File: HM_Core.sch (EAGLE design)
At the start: 7 parts

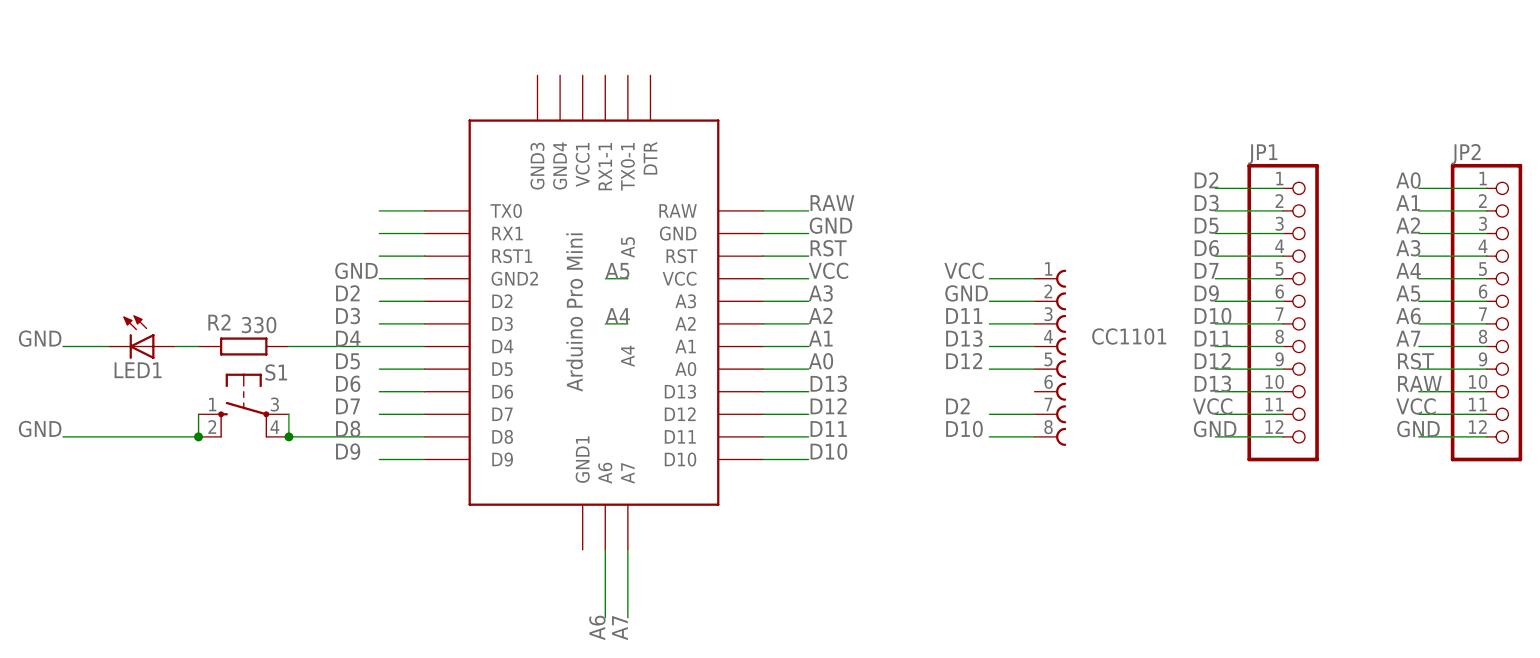
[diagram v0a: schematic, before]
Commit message: Verbesserungen
Taster zur seite raus
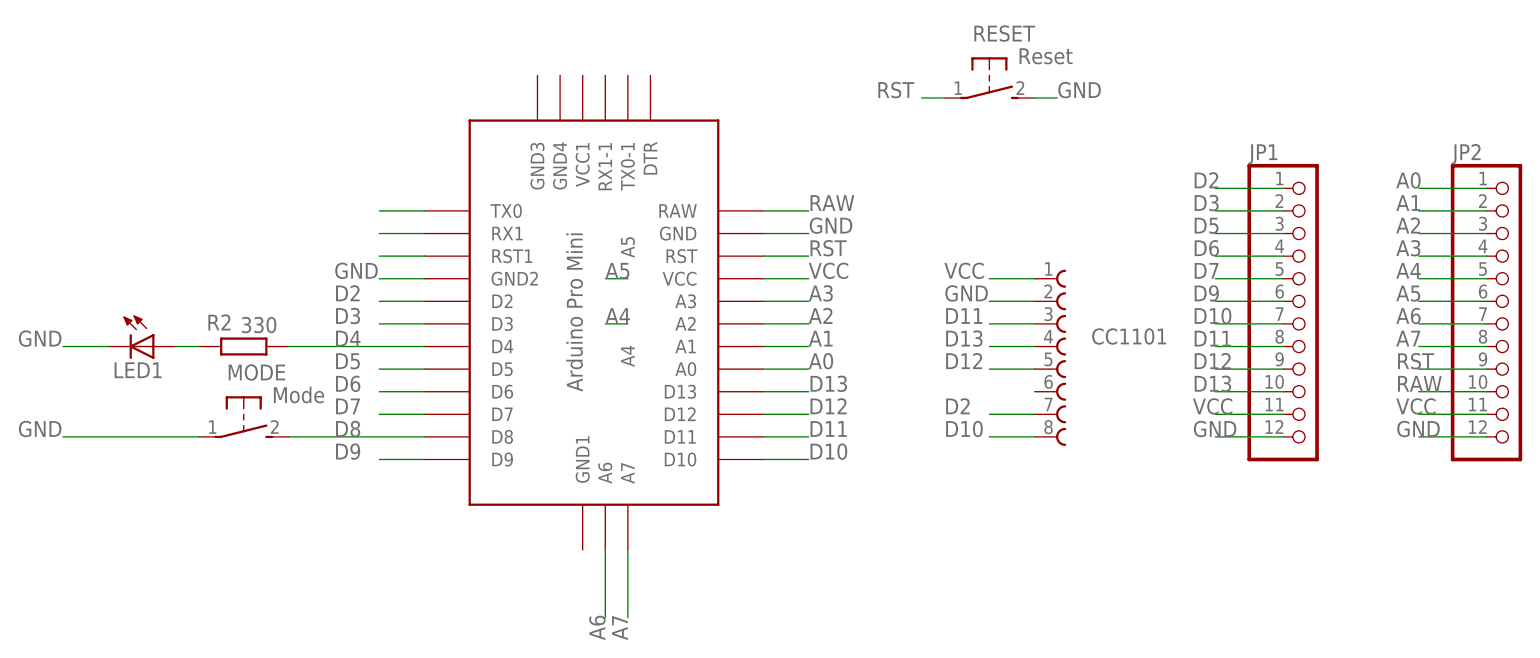
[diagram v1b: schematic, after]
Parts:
- removed S1: (no value), switch-omron:10-XX
- added MODE: Mode, switch-omron:31-XX
- added RESET: Reset, switch-omron:31-XX
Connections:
- net D8: now also MODE.S; no longer S1.P, S1.P1
- net GND: now also MODE.P, RESET.S; no longer S1.S, S1.S1
- net RST: now also RESET.P
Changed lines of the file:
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@@
 <grid distance="0.1" unitdist="inch" unit="inch" style="lines" multiple="1" display="no" altdistance="0.01" altunitdist="inch" altunit="inch"/>
 <layers>
-<layer number="1" name="Top" color="4" fill="1" visible="no" active="no"/>
-<layer number="16" name="Bottom" color="1" fill="1" visible="no" active="no"/>
-<layer number="17" name="Pads" color="2" fill="1" visible="no" active="no"/>
-<layer number="18" name="Vias" color="2" fill="1" visible="no" active="no"/>
-<layer number="19" name="Unrouted" color="6" fill="1" visible="no" active="no"/>
-<layer number="20" name="Dimension" color="15" fill="1" visible="no" active="no"/>
-<layer number="21" name="tPlace" color="7" fill="1" visible="no" active="no"/>
-<layer number="22" name="bPlace" color="7" fill="1" visible="no" active="no"/>
-<layer number="23" name="tOrigins" color="15" fill="1" visible="no" active="no"/>
-<layer number="24" name="bOrigins" color="15" fill="1" visible="no" active="no"/>
-<layer number="25" name="tNames" color="7" fill="1" visible="no" active="no"/>
-<layer number="26" name="bNames" color="7" fill="1" visible="no" active="no"/>
-<layer number="27" name="tValues" color="7" fill="1" visible="no" active="no"/>
-<layer number="28" name="bValues" color="7" fill="1" visible="no" active="no"/>
+<layer number="1" name="Top" color="4" fill="1" visible="yes" active="no"/>
+<layer number="16" name="Bottom" color="1" fill="1" visible="yes" active="no"/>
+<layer number="17" name="Pads" color="2" fill="1" visible="yes" active="no"/>
+<layer number="18" name="Vias" color="2" fill="1" visible="yes" active="no"/>
+<layer number="19" name="Unrouted" color="6" fill="1" visible="yes" active="no"/>
+<layer number="20" name="Dimension" color="24" fill="1" visible="yes" active="no"/>
+<layer number="21" name="tPlace" color="7" fill="1" visible="yes" active="no"/>
+<layer number="22" name="bPlace" color="7" fill="1" visible="yes" active="no"/>
+<layer number="23" name="tOrigins" color="15" fill="1" visible="yes" active="no"/>
+<layer number="24" name="bOrigins" color="15" fill="1" visible="yes" active="no"/>
+<layer number="25" name="tNames" color="7" fill="1" visible="yes" active="no"/>
+<layer number="26" name="bNames" color="7" fill="1" visible="yes" active="no"/>
+<layer number="27" name="tValues" color="7" fill="1" visible="yes" active="no"/>
+<layer number="28" name="bValues" color="7" fill="1" visible="yes" active="no"/>
 <layer number="29" name="tStop" color="7" fill="3" visible="no" active="no"/>
 <layer number="30" name="bStop" color="7" fill="6" visible="no" active="no"/>
@@
 <layer number="35" name="tGlue" color="7" fill="4" visible="no" active="no"/>
 <layer number="36" name="bGlue" color="7" fill="5" visible="no" active="no"/>
-<layer number="37" name="tTest" color="7" fill="1" visible="no" active="no"/>
-<layer number="38" name="bTest" color="7" fill="1" visible="no" active="no"/>
+<layer number="37" name="tTest" color="7" fill="1" visible="yes" active="no"/>
+<layer number="38" name="bTest" color="7" fill="1" visible="yes" active="no"/>
 <layer number="39" name="tKeepout" color="4" fill="11" visible="no" active="no"/>
 <layer number="40" name="bKeepout" color="1" fill="11" visible="no" active="no"/>
@@
 <layer number="44" name="Drills" color="7" fill="1" visible="no" active="no"/>
 <layer number="45" name="Holes" color="7" fill="1" visible="no" active="no"/>
-<layer number="46" name="Milling" color="3" fill="1" visible="no" active="no"/>
-<layer number="47" name="Measures" color="7" fill="1" visible="no" active="no"/>
-<layer number="48" name="Document" color="7" fill="1" visible="no" active="no"/>
-<layer number="49" name="Reference" color="7" fill="1" visible="no" active="no"/>
-<layer number="50" name="dxf" color="7" fill="1" visible="no" active="no"/>
-<layer number="51" name="tDocu" color="7" fill="1" visible="no" active="no"/>
-<layer number="52" name="bDocu" color="7" fill="1" visible="no" active="no"/>
-<layer number="53" name="tGND_GNDA" color="7" fill="9" visible="no" active="no"/>
-<layer number="54" name="bGND_GNDA" color="1" fill="9" visible="no" active="no"/>
-<layer number="56" name="wert" color="7" fill="1" visible="no" active="no"/>
-<layer number="57" name="tCAD" color="7" fill="1" visible="no" active="no"/>
-<layer number="59" name="tCarbon" color="7" fill="1" visible="no" active="no"/>
-<layer number="60" name="bCarbon" color="7" fill="1" visible="no" active="no"/>
+<layer number="46" name="Milling" color="3" fill="1" visible="yes" active="no"/>
+<layer number="47" name="Measures" color="7" fill="1" visible="yes" active="no"/>
+<layer number="48" name="Document" color="7" fill="1" visible="yes" active="no"/>
+<layer number="49" name="Reference" color="7" fill="1" visible="yes" active="no"/>
+<layer number="50" name="dxf" color="7" fill="1" visible="yes" active="no"/>
+<layer number="51" name="tDocu" color="7" fill="1" visible="yes" active="no"/>
+<layer number="52" name="bDocu" color="7" fill="1" visible="yes" active="no"/>
+<layer number="53" name="tGND_GNDA" color="7" fill="9" visible="yes" active="no"/>
+<layer number="54" name="bGND_GNDA" color="1" fill="9" visible="yes" active="no"/>
+<layer number="56" name="wert" color="7" fill="1" visible="yes" active="no"/>
+<layer number="57" name="tCAD" color="7" fill="1" visible="yes" active="no"/>
+<layer number="59" name="tCarbon" color="7" fill="1" visible="yes" active="no"/>
+<layer number="60" name="bCarbon" color="7" fill="1" visible="yes" active="no"/>
 <layer number="88" name="SimResults" color="9" fill="1" visible="yes" active="yes"/>
 <layer number="89" name="SimProbes" color="9" fill="1" visible="yes" active="yes"/>
@@
 <part name="R2" library="eagle-ltspice" library_urn="urn:adsk.eagle:library:217" deviceset="R" device="0207/10" package3d_urn="urn:adsk.eagle:package:13275/1" value="330"/>
 <part name="LED1" library="led" library_urn="urn:adsk.eagle:library:259" deviceset="LED" device="3MM" package3d_urn="urn:adsk.eagle:package:15797/1"/>
-<part name="S1" library="switch-omron" library_urn="urn:adsk.eagle:library:377" deviceset="10-XX" device="" package3d_urn="urn:adsk.eagle:package:27496/1"/>
 <part name="U$1" library="Arduino-clone" deviceset="ABK-PRO-MINI" device=""/>
 <part name="JP1" library="adafruit" library_urn="urn:adsk.eagle:library:420" deviceset="PINHD-1X12" device="" package3d_urn="urn:adsk.eagle:package:6240771/1"/>
 <part name="JP2" library="adafruit" library_urn="urn:adsk.eagle:library:420" deviceset="PINHD-1X12" device="" package3d_urn="urn:adsk.eagle:package:6240771/1"/>
 <part name="CC1101" library="Wurth_Elektronik_Electromechanic_Board_to_Board_Connectors_rev18b" library_urn="urn:adsk.eagle:library:7552989" deviceset="62000811121" device="" package3d_urn="urn:adsk.eagle:package:7553844/1"/>
+<part name="MODE" library="switch-omron" library_urn="urn:adsk.eagle:library:377" deviceset="31-XX" device="" package3d_urn="urn:adsk.eagle:package:27487/1" value="Mode"/>
+<part name="RESET" library="switch-omron" library_urn="urn:adsk.eagle:library:377" deviceset="31-XX" device="" package3d_urn="urn:adsk.eagle:package:27487/1" value="Reset"/>
 </parts>
 <sheets>
@@
 <attribute name="VALUE" x="-45.212" y="50.165" size="1.778" layer="96"/>
 </instance>
-<instance part="S1" gate="1" x="-30.48" y="48.26" smashed="yes" rot="MR270">
-<attribute name="NAME" x="-25.4" y="52.07" size="1.778" layer="95" rot="MR0"/>
-<attribute name="VALUE" x="-33.655" y="52.07" size="1.778" layer="96" rot="MR0"/>
-</instance>
 <instance part="U$1" gate="G$1" x="12.7" y="58.42" smashed="yes"/>
 <instance part="JP1" gate="G$1" x="88.9" y="60.96" smashed="yes">
@@
 <attribute name="NAME" x="64.77" y="56.118" size="1.778" layer="95"/>
 <attribute name="VALUE" x="64.77" y="53.34" size="1.778" layer="96"/>
+</instance>
+<instance part="MODE" gate="1" x="-30.48" y="45.72" smashed="yes" rot="R270">
+<attribute name="NAME" x="-32.385" y="52.07" size="1.778" layer="95"/>
+<attribute name="VALUE" x="-27.305" y="49.53" size="1.778" layer="96"/>
+</instance>
+<instance part="RESET" gate="1" x="53.34" y="83.82" smashed="yes" rot="R270">
+<attribute name="NAME" x="51.435" y="90.17" size="1.778" layer="95"/>
+<attribute name="VALUE" x="56.515" y="87.63" size="1.778" layer="96"/>
 </instance>
 </instances>
@@
 <net name="D8" class="0">
 <segment>
-<pinref part="S1" gate="1" pin="P"/>
 <wire x1="-10.16" y1="45.72" x2="-25.4" y2="45.72" width="0.1524" layer="91"/>
-<wire x1="-25.4" y1="45.72" x2="-25.4" y2="48.26" width="0.1524" layer="91"/>
-<pinref part="S1" gate="1" pin="P1"/>
-<junction x="-25.4" y="45.72"/>
 <pinref part="U$1" gate="G$1" pin="D8"/>
 <label x="-20.32" y="45.72" size="1.778" layer="95"/>
+<pinref part="MODE" gate="1" pin="S"/>
 </segment>
 </net>
@@
 </segment>
 <segment>
-<pinref part="S1" gate="1" pin="S"/>
-<wire x1="-35.56" y1="48.26" x2="-35.56" y2="45.72" width="0.1524" layer="91"/>
-<pinref part="S1" gate="1" pin="S1"/>
-<junction x="-35.56" y="45.72"/>
 <wire x1="-35.56" y1="45.72" x2="-50.8" y2="45.72" width="0.1524" layer="91"/>
 <label x="-55.88" y="45.72" size="1.778" layer="95"/>
+<pinref part="MODE" gate="1" pin="P"/>
 </segment>
 <segment>
@@
 <label x="99.06" y="45.72" size="1.778" layer="95"/>
 </segment>
+<segment>
+<pinref part="RESET" gate="1" pin="S"/>
+<wire x1="58.42" y1="83.82" x2="60.96" y2="83.82" width="0.1524" layer="91"/>
+<label x="60.96" y="83.82" size="1.778" layer="95"/>
+</segment>
 </net>
 <net name="N$2" class="0">
@@
 <label x="99.06" y="53.34" size="1.778" layer="95"/>
 </segment>
-</net>
+<segment>
+<pinref part="RESET" gate="1" pin="P"/>
+<wire x1="48.26" y1="83.82" x2="45.72" y2="83.82" width="0.1524" layer="91"/>
+<label x="40.64" y="83.82" size="1.778" layer="95"/>
+</segment>
+</net>
